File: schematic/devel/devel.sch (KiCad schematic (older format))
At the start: 40 parts, among them J1 CONN_PWR, J2 CONN_X1, J3 CONN_Y2, J4 CONN_X2, J5 CONN_Y1, U1 LM317_SOT223, U2 LM337_SOT223, U3 REF5010IDGK, U4 OPA4197

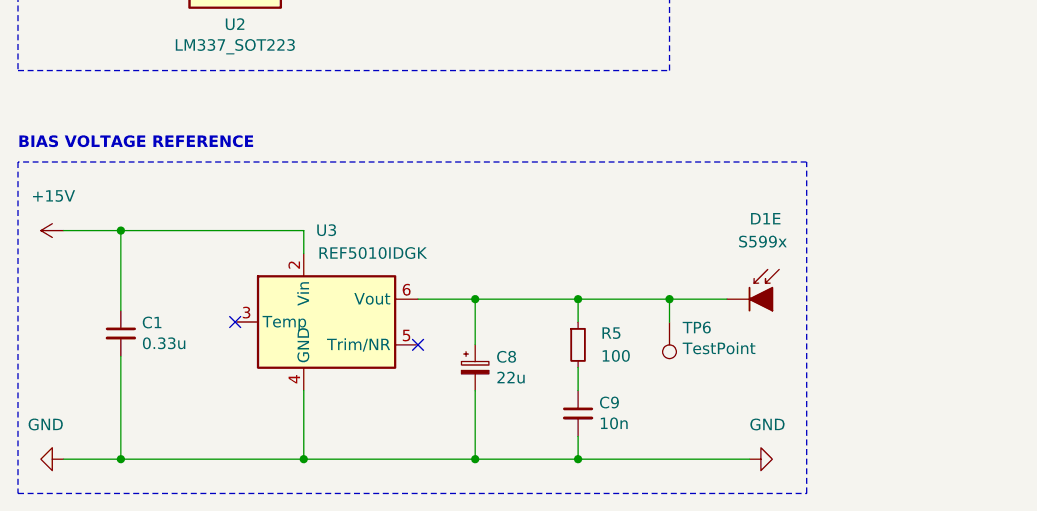
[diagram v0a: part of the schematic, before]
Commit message: completed sublayout of bias voltage reference
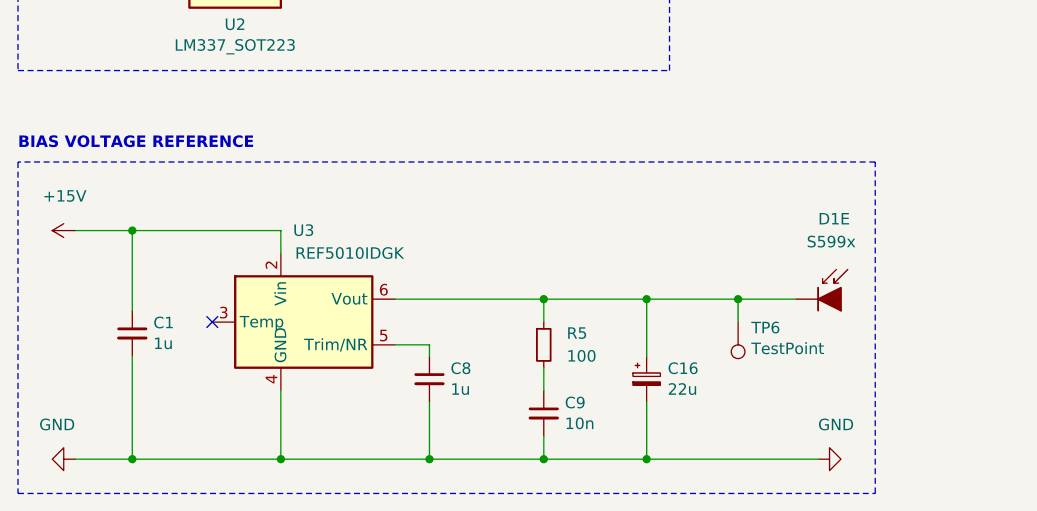
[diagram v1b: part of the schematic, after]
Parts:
- removed C8: 22u, Capacitor_SMD:CP_Elec_5x5.4, symbol Device:CP_Small
- added C16: 22u, Capacitor_SMD:CP_Elec_4x3.9, symbol Device:CP_Small
- added C8: 1u, Capacitor_SMD:C_0805_2012Metric, symbol Device:C_Small
- C1: value 0.33u -> 1u; footprint Capacitor_SMD:C_0603_1608Metric -> Capacitor_SMD:C_0805_2012Metric
- C9: footprint Capacitor_SMD:C_0603_1608Metric -> Capacitor_SMD:C_0805_2012Metric
- U3: footprint Package_SO:MSOP-8_3x3mm_P0.65mm -> Package_SO:SOIC-8_3.9x4.9mm_P1.27mm
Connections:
- net GND: now also C16.2, C8.2
- net at D1.8 (K), R5.1, TP6.1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: now also C16.1
- net at U3.5 (Trim/NR): now also C8.1
- no-connect marks 2 -> 1
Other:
- moved on the sheet: C1, C9, D1E, R5, TP6, U3
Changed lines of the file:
@@
 	9600 850  9600 4250
 Wire Wire Line
-	3350 7000 4100 7000
-Connection ~ 3350 7000
+	3650 7000 4400 7000
+Connection ~ 3650 7000
 $Comp
 L power:GND #PWR012
 U 1 1 5CA081DE
-P 4100 7000
+P 4400 7000
 AR Path="/5CA081DE" Ref="#PWR012"  Part="1"
 AR Path="/5D7CE105/5CA081DE" Ref="#PWR?"  Part="1"
-F 0 "#PWR012" H 4100 6750 50  0001 C CNN
-F 1 "GND" V 3950 7000 50  0000 R CNN
-F 2 "" H 4100 7000 50  0001 C CNN
-F 3 "" H 4100 7000 50  0001 C CNN
-	1    4100 7000
+F 0 "#PWR012" H 4400 6750 50  0001 C CNN
+F 1 "GND" V 4250 7000 50  0000 R CNN
+F 2 "" H 4400 7000 50  0001 C CNN
+F 3 "" H 4400 7000 50  0001 C CNN
+	1    4400 7000
 	0    -1   1    0
 $EndComp
 Wire Wire Line
-	3750 6300 4000 6300
-Wire Wire Line
-	3350 6700 3350 6600
-Wire Wire Line
-	1350 7000 1100 7000
-Connection ~ 1350 7000
-Wire Wire Line
-	1350 6550 1350 7000
+	4050 6300 4300 6300
+Wire Wire Line
+	1400 7000 1150 7000
+Connection ~ 1400 7000
+Wire Wire Line
+	1400 6550 1400 7000
 $Comp
 L Device:C_Small C1
 U 1 1 5CA08266
-P 1350 6450
+P 1400 6450
 AR Path="/5CA08266" Ref="C1"  Part="1"
 AR Path="/5D7CE105/5CA08266" Ref="C?"  Part="1"
-F 0 "C1" H 1442 6496 50  0000 L CNN
-F 1 "0.33u" H 1442 6405 50  0000 L CNN
-F 2 "Capacitor_SMD:C_0603_1608Metric" H 1350 6450 50  0001 C CNN
-F 3 "~" H 1350 6450 50  0001 C CNN
-	1    1350 6450
-	1    0    0    -1
-$EndComp
-Wire Wire Line
-	1100 6000 1350 6000
-Connection ~ 1350 6000
+F 0 "C1" H 1492 6496 50  0000 L CNN
+F 1 "1u" H 1492 6405 50  0000 L CNN
+F 2 "Capacitor_SMD:C_0805_2012Metric" H 1400 6450 50  0001 C CNN
+F 3 "~" H 1400 6450 50  0001 C CNN
+	1    1400 6450
+	1    0    0    -1
+$EndComp
+Wire Wire Line
+	1150 6000 1400 6000
+Connection ~ 1400 6000
 $Comp
 L power:GND #PWR02
 U 1 1 5CA0825E
-P 1100 7000
+P 1150 7000
 AR Path="/5CA0825E" Ref="#PWR02"  Part="1"
 AR Path="/5D7CE105/5CA0825E" Ref="#PWR?"  Part="1"
-F 0 "#PWR02" H 1100 6750 50  0001 C CNN
-F 1 "GND" V 1250 7000 50  0000 R CNN
-F 2 "" H 1100 7000 50  0001 C CNN
-F 3 "" H 1100 7000 50  0001 C CNN
-	1    1100 7000
+F 0 "#PWR02" H 1150 6750 50  0001 C CNN
+F 1 "GND" V 1300 7000 50  0000 R CNN
+F 2 "" H 1150 7000 50  0001 C CNN
+F 3 "" H 1150 7000 50  0001 C CNN
+	1    1150 7000
 	0    1    -1   0
 $EndComp
@@
 L power:+15V #PWR01
 U 1 1 5CA08258
-P 1100 6000
+P 1150 6000
 AR Path="/5CA08258" Ref="#PWR01"  Part="1"
 AR Path="/5D7CE105/5CA08258" Ref="#PWR?"  Part="1"
-F 0 "#PWR01" H 1100 5850 50  0001 C CNN
-F 1 "+15V" V 950 5950 50  0000 L CNN
-F 2 "" H 1100 6000 50  0001 C CNN
-F 3 "" H 1100 6000 50  0001 C CNN
-	1    1100 6000
+F 0 "#PWR01" H 1150 5850 50  0001 C CNN
+F 1 "+15V" V 1000 5950 50  0000 L CNN
+F 2 "" H 1150 6000 50  0001 C CNN
+F 3 "" H 1150 6000 50  0001 C CNN
+	1    1150 6000
 	0    -1   1    0
 $EndComp
@@
 L Reference_Voltage:REF5010IDGK U3
 U 1 1 5CA081E7
-P 2250 6400
+P 2150 6400
 AR Path="/5CA081E7" Ref="U3"  Part="1"
 AR Path="/5D7CE105/5CA081E7" Ref="U?"  Part="1"
-F 0 "U3" H 2250 6800 50  0000 C CNN
-F 1 "REF5010IDGK" H 2450 6700 50  0000 C CNN
-F 2 "Package_SO:MSOP-8_3x3mm_P0.65mm" H 2300 6150 50  0001 L CIN
-F 3 "http://www.ti.com/lit/ds/symlink/ref5030.pdf" H 2250 6400 50  0001 C CIN
-	1    2250 6400
-	1    0    0    -1
-$EndComp
-NoConn ~ 1850 6400
-NoConn ~ 2650 6500
-Wire Wire Line
-	1350 6000 1350 6350
-Wire Wire Line
-	2650 6300 2900 6300
-Connection ~ 2900 6300
-$Comp
-L Device:CP_Small C8
-U 1 1 5CA081D0
-P 2900 6600
-AR Path="/5CA081D0" Ref="C8"  Part="1"
-AR Path="/5D7CE105/5CA081D0" Ref="C?"  Part="1"
-F 0 "C8" H 2992 6646 50  0000 L CNN
-F 1 "22u" H 2992 6555 50  0000 L CNN
-F 2 "Capacitor_SMD:CP_Elec_5x5.4" H 2900 6600 50  0001 C CNN
-F 3 "~" H 2900 6600 50  0001 C CNN
-	1    2900 6600
-	1    0    0    -1
-$EndComp
-Wire Wire Line
-	2900 6500 2900 6300
-Wire Wire Line
-	2900 6300 3350 6300
-Connection ~ 3350 6300
-Wire Wire Line
-	2900 6700 2900 7000
-Connection ~ 2900 7000
-Wire Wire Line
-	2900 7000 3350 7000
-Wire Wire Line
-	2150 7000 2900 7000
-Wire Wire Line
-	1350 6000 2150 6000
-Wire Wire Line
-	2150 6000 2150 6100
-Wire Wire Line
-	1350 7000 2150 7000
-Connection ~ 2150 7000
-Wire Wire Line
-	2150 7000 2150 6700
+F 0 "U3" H 2150 6800 50  0000 C CNN
+F 1 "REF5010IDGK" H 2350 6700 50  0000 C CNN
+F 2 "Package_SO:SOIC-8_3.9x4.9mm_P1.27mm" H 2200 6150 50  0001 L CIN
+F 3 "http://www.ti.com/lit/ds/symlink/ref5030.pdf" H 2150 6400 50  0001 C CIN
+	1    2150 6400
+	1    0    0    -1
+$EndComp
+NoConn ~ 1750 6400
+Wire Wire Line
+	1400 6000 1400 6350
+Wire Wire Line
+	2550 6300 3200 6300
+Connection ~ 3200 6300
+Wire Wire Line
+	3200 6400 3200 6300
+Wire Wire Line
+	3200 6300 3650 6300
+Connection ~ 3650 6300
+Wire Wire Line
+	3200 6600 3200 6700
+Connection ~ 3200 7000
+Wire Wire Line
+	3200 7000 3650 7000
+Wire Wire Line
+	2050 7000 2700 7000
+Wire Wire Line
+	1400 6000 2050 6000
+Wire Wire Line
+	2050 6000 2050 6100
+Wire Wire Line
+	1400 7000 2050 7000
+Connection ~ 2050 7000
+Wire Wire Line
+	2050 7000 2050 6700
 $Comp
 L Device:C_Small C9
 U 1 1 5CA081BE
-P 3350 6800
+P 3200 6800
 AR Path="/5CA081BE" Ref="C9"  Part="1"
 AR Path="/5D7CE105/5CA081BE" Ref="C?"  Part="1"
-F 0 "C9" H 3442 6846 50  0000 L CNN
-F 1 "10n" H 3442 6755 50  0000 L CNN
-F 2 "Capacitor_SMD:C_0603_1608Metric" H 3350 6800 50  0001 C CNN
-F 3 "~" H 3350 6800 50  0001 C CNN
-	1    3350 6800
+F 0 "C9" H 3292 6846 50  0000 L CNN
+F 1 "10n" H 3292 6755 50  0000 L CNN
+F 2 "Capacitor_SMD:C_0805_2012Metric" H 3200 6800 50  0001 C CNN
+F 3 "~" H 3200 6800 50  0001 C CNN
+	1    3200 6800
 	1    0    0    -1
 $EndComp
@@
 L Device:R_Small R5
 U 1 1 5CA081B8
-P 3350 6500
+P 3200 6500
 AR Path="/5CA081B8" Ref="R5"  Part="1"
 AR Path="/5D7CE105/5CA081B8" Ref="R?"  Part="1"
-F 0 "R5" H 3450 6550 50  0000 L CNN
-F 1 "100" H 3450 6450 50  0000 L CNN
-F 2 "Resistor_SMD:R_0805_2012Metric" H 3350 6500 50  0001 C CNN
-F 3 "~" H 3350 6500 50  0001 C CNN
-	1    3350 6500
-	1    0    0    -1
-$EndComp
-Wire Wire Line
-	3350 6400 3350 6300
-Wire Wire Line
-	3350 6300 3750 6300
-Connection ~ 3750 6300
-Wire Wire Line
-	3350 6900 3350 7000
+F 0 "R5" H 3300 6550 50  0000 L CNN
+F 1 "100" H 3300 6450 50  0000 L CNN
+F 2 "Resistor_SMD:R_0805_2012Metric" H 3200 6500 50  0001 C CNN
+F 3 "~" H 3200 6500 50  0001 C CNN
+	1    3200 6500
+	1    0    0    -1
+$EndComp
+Wire Wire Line
+	3650 6300 4050 6300
+Connection ~ 4050 6300
 $Comp
 L Connector:TestPoint TP6
 U 1 1 5CA081AC
-P 3750 6400
+P 4050 6400
 AR Path="/5CA081AC" Ref="TP6"  Part="1"
 AR Path="/5D7CE105/5CA081AC" Ref="TP?"  Part="1"
-F 0 "TP6" H 3692 6426 50  0000 R CNN
-F 1 "TestPoint" H 3692 6517 50  0000 R CNN
-F 2 "TestPoint:TestPoint_Pad_D1.0mm" H 3950 6400 50  0001 C CNN
-F 3 "~" H 3950 6400 50  0001 C CNN
-	1    3750 6400
+F 0 "TP6" H 3992 6426 50  0000 R CNN
+F 1 "TestPoint" H 3992 6517 50  0000 R CNN
+F 2 "TestPoint:TestPoint_Pad_D1.0mm" H 4250 6400 50  0001 C CNN
+F 3 "~" H 4250 6400 50  0001 C CNN
+	1    4050 6400
 	-1   0    0    1
 $EndComp
 Wire Wire Line
-	3750 6400 3750 6300
+	4050 6400 4050 6300
 Wire Notes Line
-	900  7150 4350 7150
+	900  7150 4650 7150
 Wire Notes Line
-	4350 7150 4350 5700
+	4650 7150 4650 5700
 Wire Notes Line
-	4350 5700 900  5700
+	4650 5700 900  5700
 Wire Notes Line
 	900  5700 900  7150
@@
 L Sensor_OpticalPosition:S599x D?
 U 5 1 5C9FE408
-P 4200 6300
+P 4500 6300
 AR Path="/5D929D0E/5C9FE408" Ref="D?"  Part="5"
 AR Path="/5C9FE408" Ref="D1"  Part="5"
-F 0 "D1" H 4100 6650 50  0000 L CNN
-F 1 "S599x" H 4050 6550 50  0000 L CNN
-F 2 "Sensor_OpticalPosition:S5990" H 4150 6300 50  0001 C CNN
-F 3 "~" H 4150 6300 50  0001 C CNN
-	5    4200 6300
+F 0 "D1" H 4400 6650 50  0000 L CNN
+F 1 "S599x" H 4350 6550 50  0000 L CNN
+F 2 "Sensor_OpticalPosition:S5990" H 4450 6300 50  0001 C CNN
+F 3 "~" H 4450 6300 50  0001 C CNN
+	5    4500 6300
 	1    0    0    -1
 $EndComp
@@
 Wire Wire Line
 	2750 4150 3450 4150
+Wire Wire Line
+	2550 6500 2700 6500
+Wire Wire Line
+	2700 6500 2700 6550
+Connection ~ 2700 7000
+Wire Wire Line
+	2700 7000 3200 7000
+$Comp
+L Device:C_Small C8
+U 1 1 5D2EFB17
+P 2700 6650
+AR Path="/5D2EFB17" Ref="C8"  Part="1"
+AR Path="/5D7CE105/5D2EFB17" Ref="C?"  Part="1"
+F 0 "C8" H 2792 6696 50  0000 L CNN
+F 1 "1u" H 2792 6605 50  0000 L CNN
+F 2 "Capacitor_SMD:C_0805_2012Metric" H 2700 6650 50  0001 C CNN
+F 3 "~" H 2700 6650 50  0001 C CNN
+	1    2700 6650
+	1    0    0    -1
+$EndComp
+Wire Wire Line
+	2700 6750 2700 7000
+Wire Wire Line
+	3200 6900 3200 7000
+$Comp
+L Device:CP_Small C16
+U 1 1 5D2F9437
+P 3650 6650
+AR Path="/5D2F9437" Ref="C16"  Part="1"
+AR Path="/5D7CE105/5D2F9437" Ref="C?"  Part="1"
+F 0 "C16" H 3742 6696 50  0000 L CNN
+F 1 "22u" H 3742 6605 50  0000 L CNN
+F 2 "Capacitor_SMD:CP_Elec_4x3.9" H 3650 6650 50  0001 C CNN
+F 3 "~" H 3650 6650 50  0001 C CNN
+	1    3650 6650
+	1    0    0    -1
+$EndComp
+Wire Wire Line
+	3650 6300 3650 6550
+Wire Wire Line
+	3650 6750 3650 7000
 $EndSCHEMATC

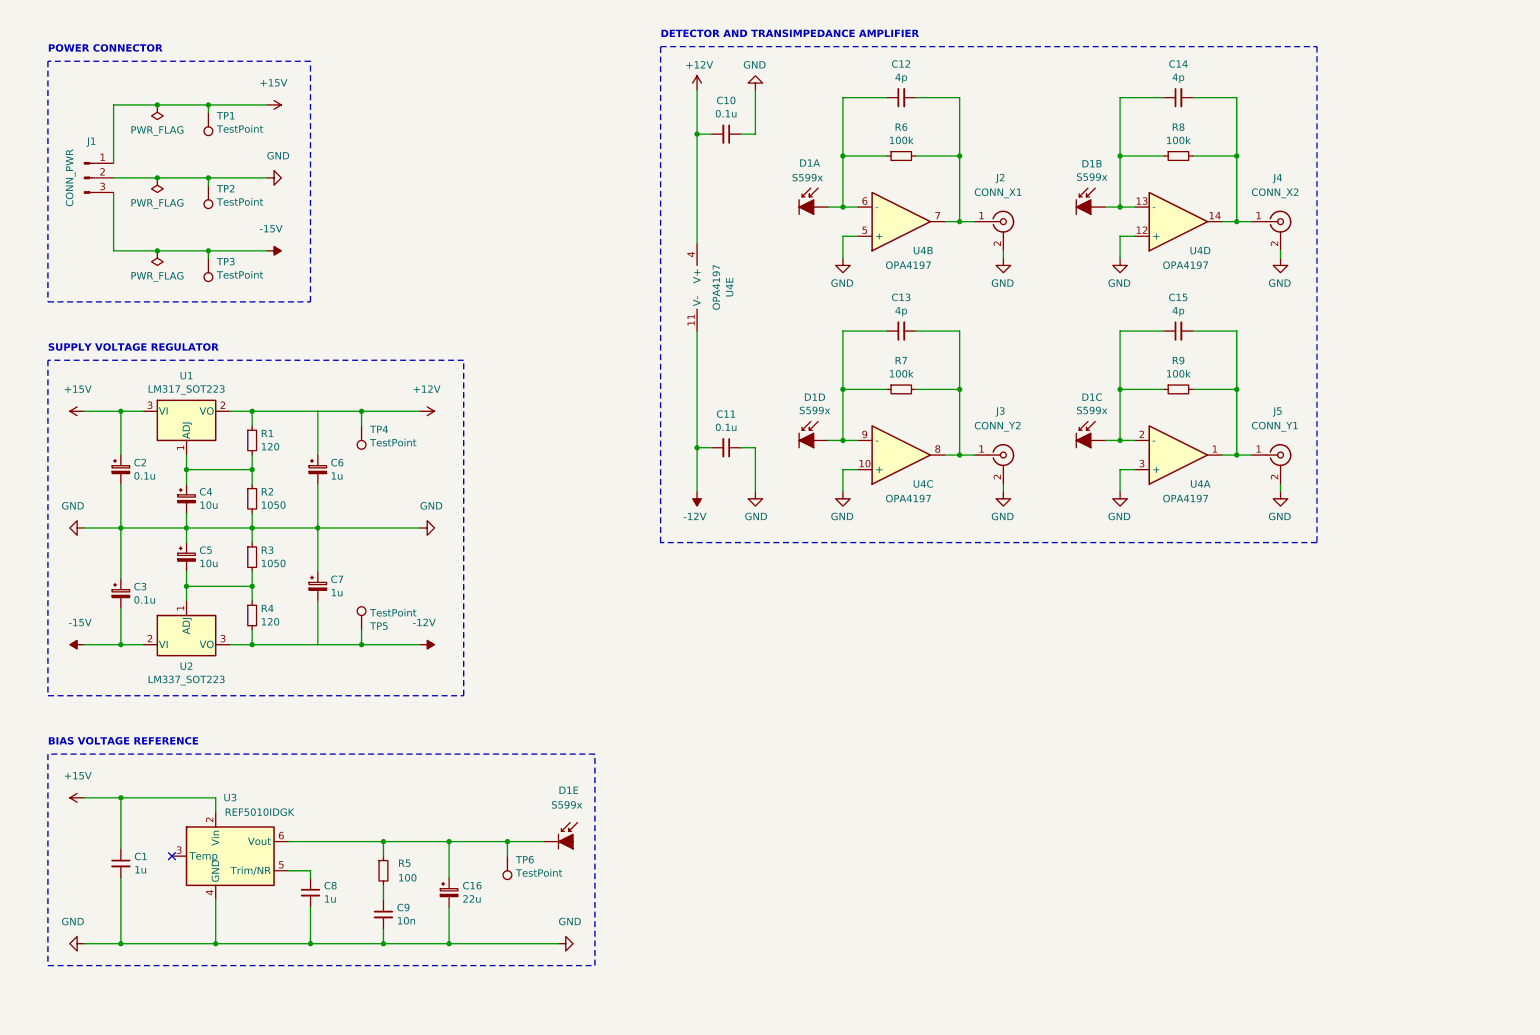
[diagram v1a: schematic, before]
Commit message: added mosfet polarity protection to power connector
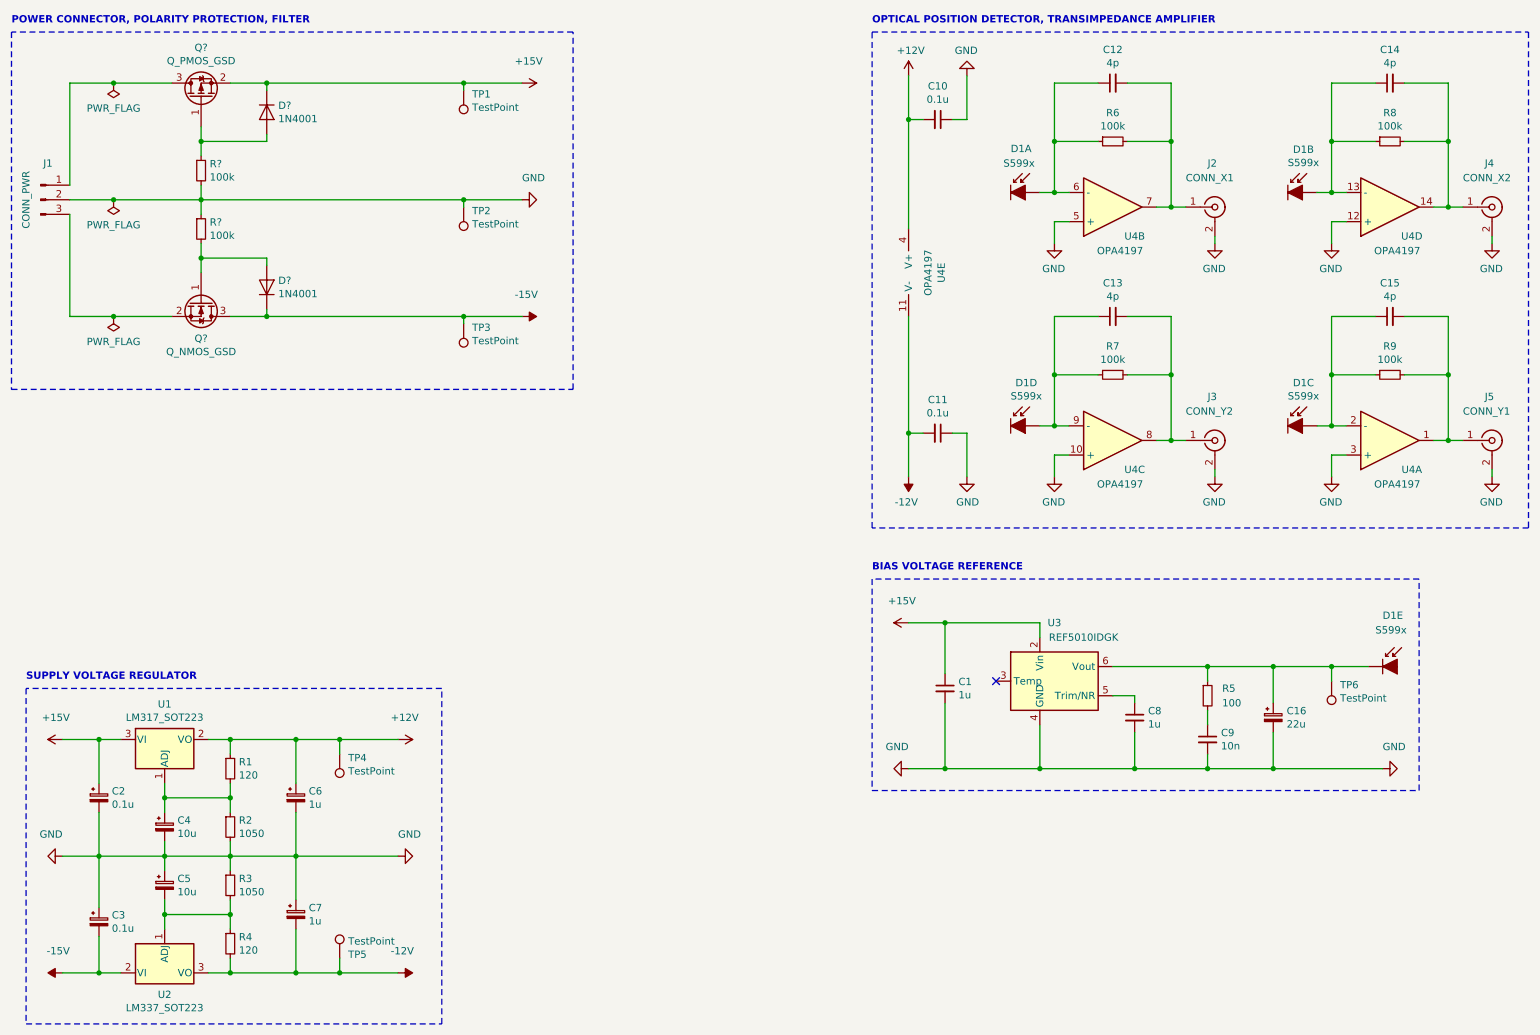
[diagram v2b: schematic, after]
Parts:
- added D? (x2): 1N4001, Diode_THT:D_DO-41_SOD81_P10.16mm_Horizontal, symbol Diode:1N4001
- added Q?: Q_PMOS_GSD, symbol Device:Q_PMOS_GSD
- added Q?: Q_NMOS_GSD, symbol Device:Q_NMOS_GSD
- added R? (x2): 100k, symbol Device:R_Small
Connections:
- net +15V: now also D?.1 (K), Q?.2 (S); no longer J1.1 (Pin_1)
- net -15V: now also D?.1 (K), Q?.3 (D); no longer J1.3 (Pin_3)
- net GND: now also R?.1, R?.2
- new net: J1.1 (Pin_1), Q?.3 (D)
- new net: J1.3 (Pin_3), Q?.2 (S)
- new net: D?.2 (A), Q?.1 (G), R?.1
- new net: D?.2 (A), Q?.1 (G), R?.2
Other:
- note added: "OPTICAL POSITION DETECTOR, TRANSIMPEDANCE AMPLIFIER"
- note added: "POWER CONNECTOR, POLARITY PROTECTION, FILTER"
- note removed: "DETECTOR AND TRANSIMPEDANCE AMPLIFIER"
- note removed: "POWER CONNECTOR"
- moved on the sheet: C1, C10, C11, C12, C13, C14, C15, C16, C2, C3, C4, C5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
